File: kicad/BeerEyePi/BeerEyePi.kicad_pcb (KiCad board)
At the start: 2 copper layers, 65 x 63 mm, 72 parts, among them J1 RaspberryPi, J2 Extension, J3 RGB_LED, J4 TransSensor, J5 RGB_LED, J6 RGB_LED, J7 TransSensor, Q1 IRLML2502, Q2 IRLML2502, Q3 IRLML2502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

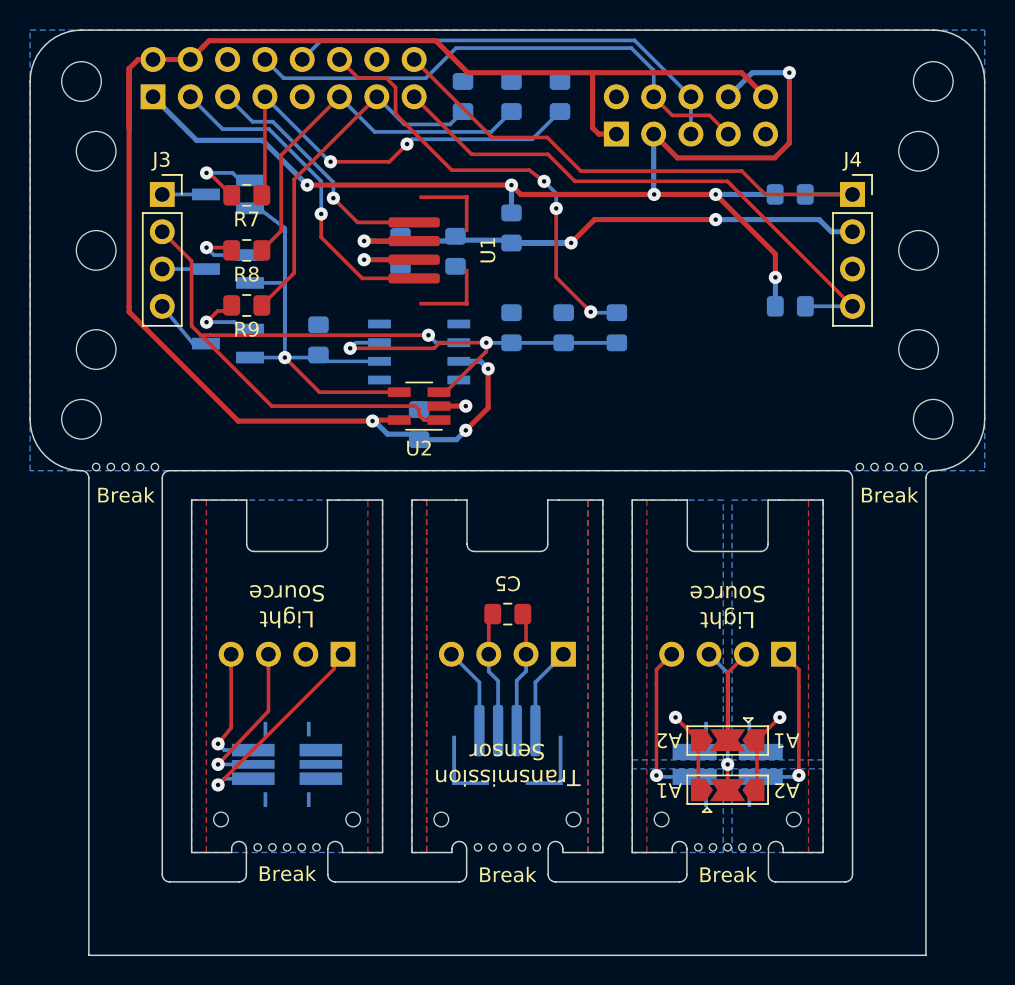
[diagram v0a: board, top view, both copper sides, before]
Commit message: Modules are individual KiCAD projects now.
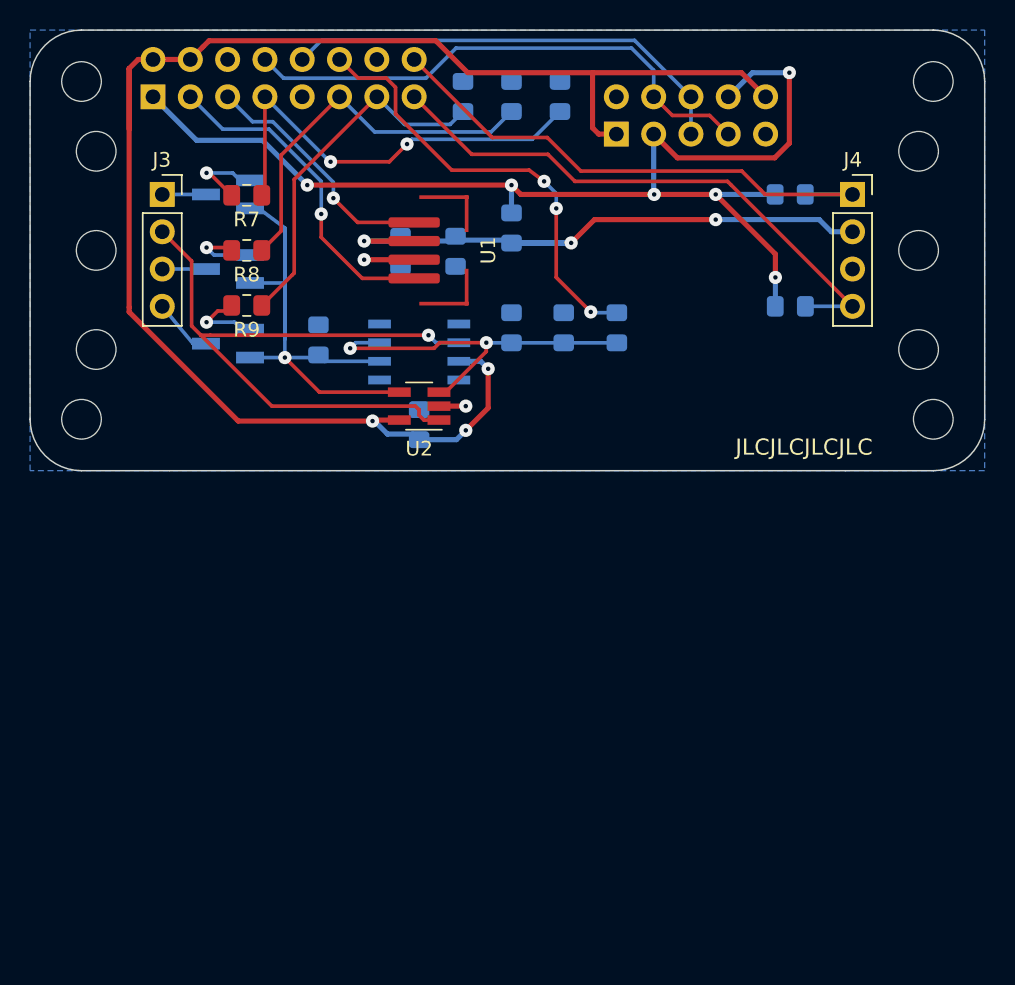
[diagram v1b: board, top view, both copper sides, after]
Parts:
- removed C5: 100n, Capacitor_SMD:C_0805_2012Metric_Pad1.15x1.40mm_HandSolder
- removed D1: LED_RGB, LED-PLCC:PLCC6-3528
- removed D2: LED_ABGR, LED-PLCC:PLCC4-3528
- removed H1, H2, H3, H4, H5, H6: RecoveryHole, Drill:Drill_1.0mm
- removed J5, J6: RGB_LED, Connector_PinHeader_2.54mm:PinHeader_1x04_P2.54mm_Horizontal
- removed J7: TransSensor, Connector_PinHeader_2.54mm:PinHeader_1x04_P2.54mm_Horizontal
- removed JP1: CA2, Jumper:SolderJumper-3_P2.0mm_Open_TrianglePad1.0x1.5mm
- removed JP2: CA1, Jumper:SolderJumper-3_P2.0mm_Open_TrianglePad1.0x1.5mm
- removed REF** (x25): Drill_0.5mm, Drill:Drill_0.5mm
- removed U4: VEML7700, VEML:VEML7700_HandSoldering
- Q1, Q2, Q3: value IRLML2502 -> CPH3456
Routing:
- net Net-(D1-Pad1): track 15.0 -> 0.00 mm, vias 1 -> 0
- net /PLCC4_3: track 11.3 -> 0.00 mm, vias 1 -> 0
- net /PLCC4_4: track 11.3 -> 0.00 mm, vias 1 -> 0
- net Net-(D1-Pad2): track 11.3 -> 0.00 mm, vias 1 -> 0
- net Net-(J6-Pad3): track 9.78 -> 0.00 mm, vias 1 -> 0
- net Net-(D1-Pad3): track 8.99 -> 0.00 mm, vias 1 -> 0
- net Net-(C5-Pad2): track 8.66 -> 0.00 mm
- net Net-(C5-Pad1): track 8.64 -> 0.00 mm
- net Net-(J6-Pad2): track 6.38 -> 0.00 mm
- net Net-(J7-Pad4): track 6.34 -> 0.00 mm
- net Net-(J7-Pad1): track 6.34 -> 0.00 mm
- net /PLCC4_2: track 5.59 -> 0.00 mm, vias 1 -> 0
- net /PLCC4_1: track 5.59 -> 0.00 mm, vias 1 -> 0
- removed copper zone on B.Cu, net (none)
- removed copper zone on F.Cu, net (none)
- removed copper zone on B.Cu, net /PLCC4_1
- removed copper zone on B.Cu, net /PLCC4_2
- removed copper zone on B.Cu, net /PLCC4_3
- removed copper zone on B.Cu, net /PLCC4_4
- removed copper zone on B.Cu, net /PLCC6_ANODE
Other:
- board size 65 x 63 mm -> 65 x 30 mm
- board text added: "Beer Eye 0.1b rev.0 by H.-C. Ahlswede https://github.com/beer-eye"
- board text added: "JLCJLCJLCJLC"
- board text removed: "A1"
- board text removed: "A2"
- board text removed: "Beer Eye 0.1a rev.1 by H.-C. Ahlswede https://github.com/beer-eye"
- board text removed: "Break"
- board text removed: "Light Source"
- board text removed: "Transmission Sensor"
